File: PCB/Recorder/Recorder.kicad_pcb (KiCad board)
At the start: 2 copper layers, 70 x 70 mm, 47 parts, among them J1 Battery, J2 Reset, J3 TC2030-USB-NL-DS, J4 TF_PUSH, J5 USB-C-Socket-H, Q2 CJ2301, SW1 SW_Push, U1 R, U2 L, U3 TP4054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

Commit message: Tidy readme
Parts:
- U4: footprint Package_TO_SOT_SMD:SOT-23-5 -> RevK:SOT-23-5

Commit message: Fucking KiCAD changes
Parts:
- J5: value USB-C-Socket-H -> USB-C-Socket-V
- U1, U2: footprint RevK:ICS43434_MEMS_Mic -> RevK:ICS43434_MEMS_Mic_Open

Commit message: PCB Update
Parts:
- J5: value USB-C-Socket-V -> USB-C-Socket-H

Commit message: Tidy
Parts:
- moved R8 1.81 mm to (113.8, 103.0), turned to 0 degrees
- moved J3 0.77 mm to (111.7, 104.1)
- moved C1 0.77 mm to (111.5, 104.3)
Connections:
- J3 pad 2: VBUS -> D-
- J3 pad 6: GND -> D-
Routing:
- net GND: track 55.6 -> 47.8 mm, vias 41 -> 39
- net D-: track 36.4 -> 38.9 mm
- net BLINK: track 11.4 -> 9.88 mm
- net D+: track 27.9 -> 28.9 mm
- net +3V3: track 118.6 -> 119.5 mm
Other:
- board text added: "TC2030"

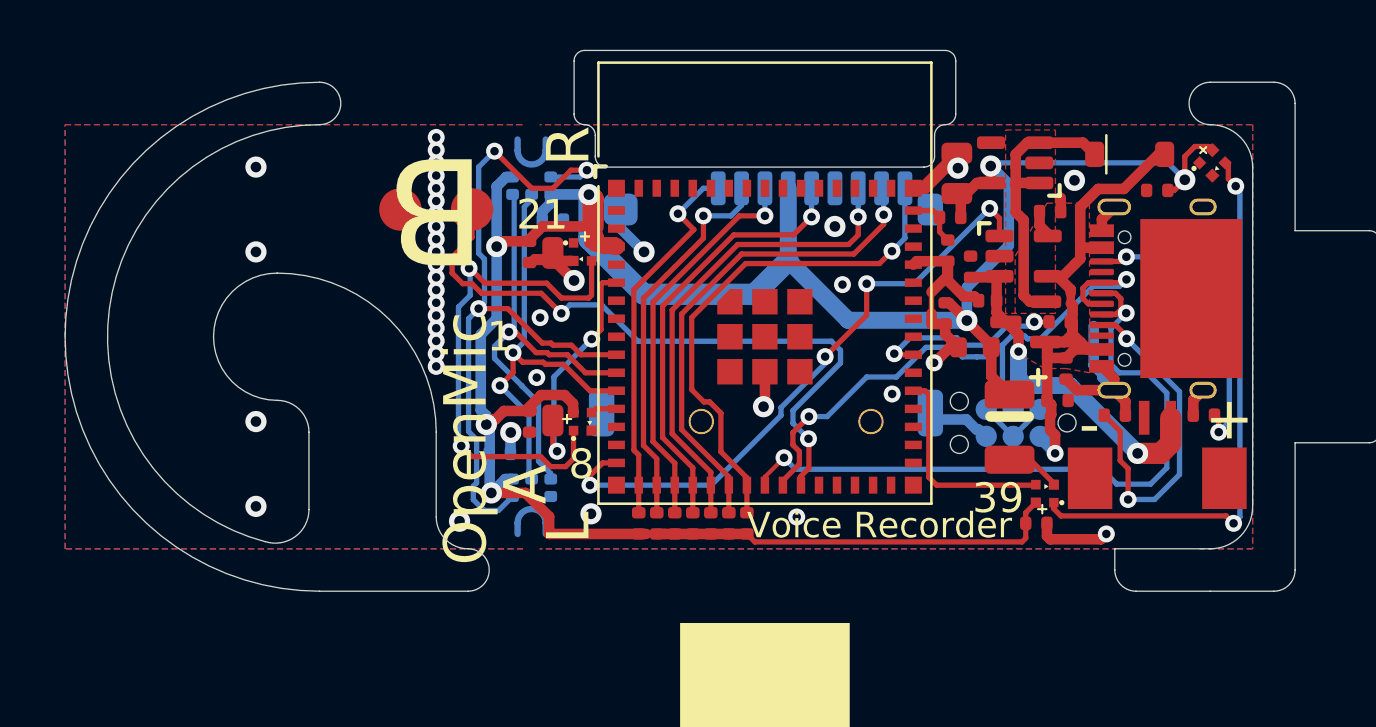
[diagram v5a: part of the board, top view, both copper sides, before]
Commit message: Power control for LEDs
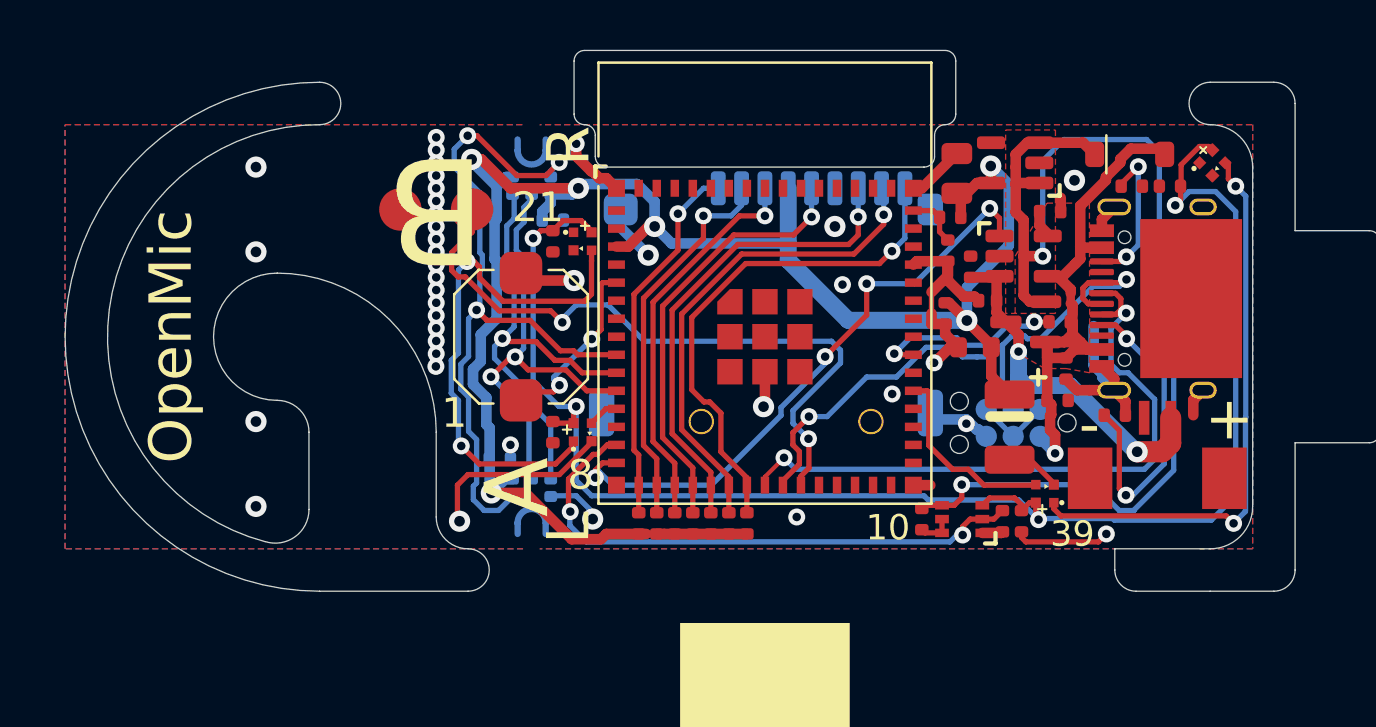
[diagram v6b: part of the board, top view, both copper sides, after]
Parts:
- removed SW1: SW_Push, RevK:TS-1092S-B3D2-G
- added R15: 10K, RevK:R_0402, F.Cu at (111.2, 108.7)
- added R18: 10K, RevK:R_0402, F.Cu at (107.4, 108.6)
- added SW2: SW_SPST, Button_Switch_SMD:SW_Push_1TS009xxxx-xxxx-xxxx_6x6x5mm, F.Cu at (88.5, 100.0)
- added U5: NX6020CAKS, RevK:SOT-363_SC-70-6, F.Cu at (109.3, 108.6)
- U6: value ESP32-S3-MINI-1 -> ESP32-S3-MINI-1-N4R2
- moved R6 11.3 mm to (117.3, 92.9), turned to 180 degrees
- moved C5 1.21 mm to (90.0, 104.5)
- moved C6 1.21 mm to (90.0, 95.5)
- moved C4 0.71 mm to (112.1, 108.7), turned to -90 degrees
- moved C10 0.63 mm to (119.1, 92.9)
- moved D4 0.50 mm to (91.4, 95.5)
- moved D5 0.50 mm to (91.4, 104.5)
- moved C13 0.25 mm to (87.5, 105.8)
- moved C16 0.10 mm to (109.0, 92.3)
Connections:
- net Net-(D3-K) renamed VIN
- C10 pad 1: +3V3 -> VLED
- C4 pad 1: +3V3 -> VLED
- C5 pad 1: +3V3 -> VLED
- C6 pad 1: +3V3 -> VLED
- D1 pad 2: +3V3 -> VLED
- D4 pad 2: +3V3 -> VLED
- D5 pad 2: +3V3 -> VLED
- D6 pad 2: +3V3 -> VLED
- U6 pad 14: unconnected-(U6-GPIO10-Pad14) -> PLED
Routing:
- net VLED: track 0.00 -> 75.3 mm, vias 0 -> 4
- net VIN: track 13.3 -> 54.1 mm, vias 0 -> 2
- net +3V3: track 119.5 -> 84.5 mm, vias 7 -> 6
- net PLED: track 0.00 -> 27.2 mm, vias 0 -> 2
- net GND: track 47.8 -> 60.5 mm, vias 39 -> 38
- net Net-(J5-CC2): track 14.2 -> 6.98 mm
- net BUTTON: track 11.1 -> 8.68 mm
- net D-: track 38.9 -> 36.8 mm
- net Net-(U5A-D): track 0.00 -> 1.66 mm
- net Net-(J5-CC1): track 16.3 -> 14.7 mm
- net BLINK: track 9.88 -> 9.06 mm
- net Net-(D4-I): track 23.8 -> 24.6 mm
- net SDDAT2: track 18.1 -> 17.4 mm
- net SD: track 20.3 -> 20.9 mm
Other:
- board text added: "10"
- board text removed: "Voice Recorder"

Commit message: Clean up
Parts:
- U4: footprint RevK:SOT-23-5 -> RevK:SOT-23-5-90
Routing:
- net GND: track 60.5 -> 55.7 mm, vias 38 -> 41
- net +3V3: track 84.5 -> 86.5 mm
- net VIN: track 54.1 -> 52.8 mm
- net Net-(J5-CC1): track 14.7 -> 13.9 mm
- net VLED: track 75.3 -> 75.9 mm
- net BUTTON: track 8.68 -> 8.11 mm
